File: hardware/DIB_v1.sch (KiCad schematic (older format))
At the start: 8 parts, among them IC4 M24C32-WMN6P, J1 20-pin power socket, J17 FTDI, J3 28-pin module socket

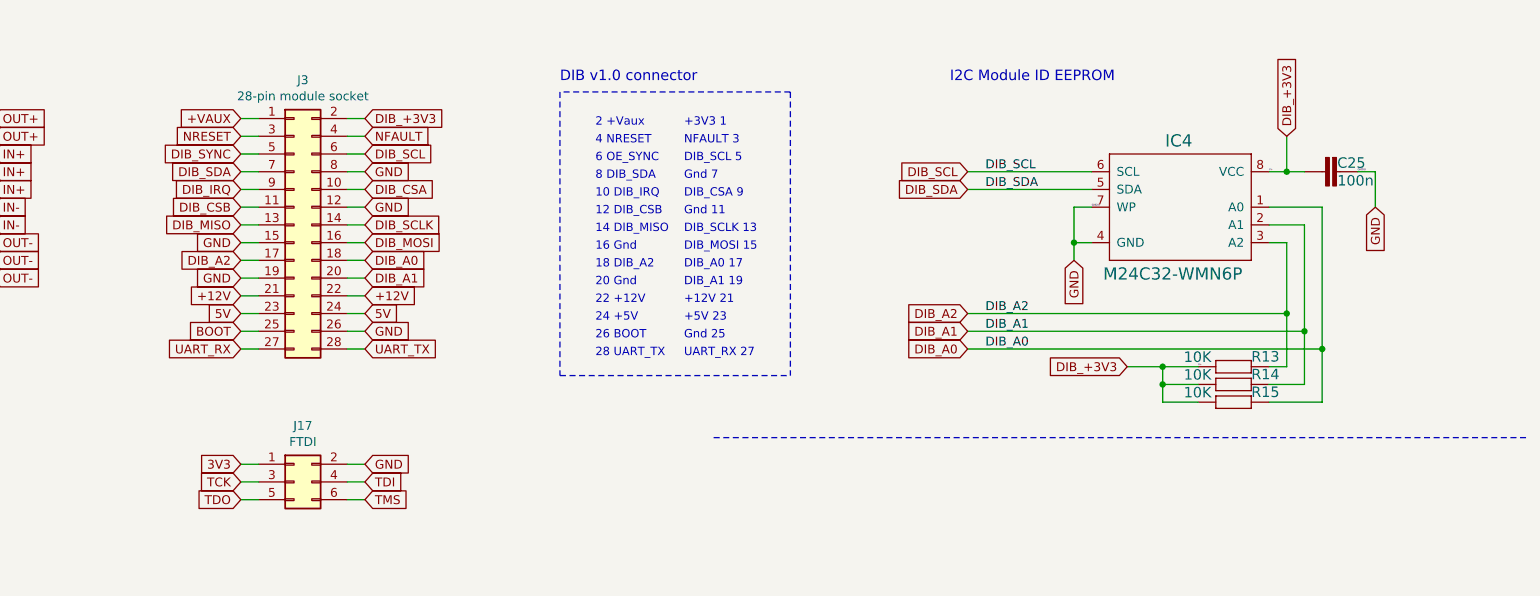
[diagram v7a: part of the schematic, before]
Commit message: Before AGND - GND
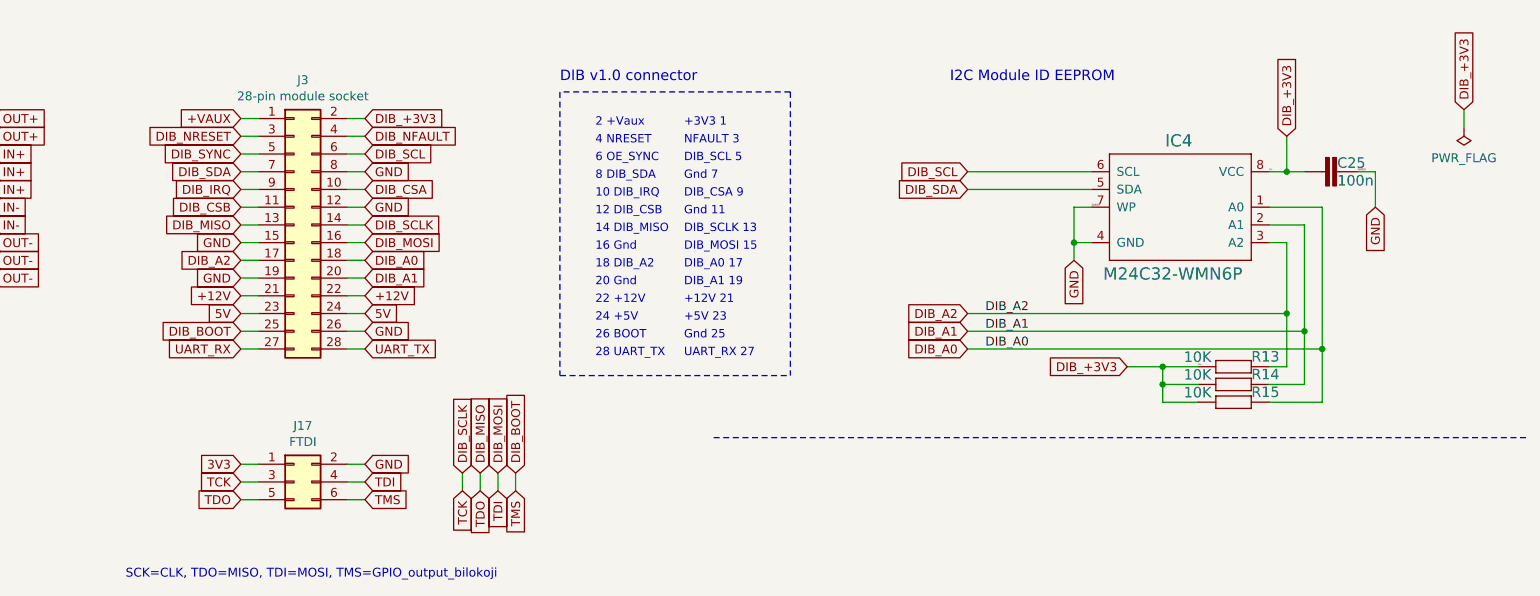
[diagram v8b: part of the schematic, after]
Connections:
- net TCK is gone; now on net DIB_SCLK: J17.3 (Pin_3)
- net TDI is gone; now on net DIB_MOSI: J17.4 (Pin_4)
- net TDO is gone; now on net DIB_MISO: J17.5 (Pin_5)
- net TMS is gone; now on net DIB_BOOT: J17.6 (Pin_6)
- net BOOT renamed DIB_BOOT
- net NFAULT renamed DIB_NFAULT
- net NRESET renamed DIB_NRESET
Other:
- note added: "SCK=CLK, TDO=MISO, TDI=MOSI, TMS=GPIO_output_bilokoji"
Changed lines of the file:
@@
 +VAUX
 Text GLabel 3600 1150 0    50   Input ~ 0
-NRESET
+DIB_NRESET
 Text GLabel 3600 1250 0    50   Input ~ 0
 DIB_SYNC
@@
 5V
 Text GLabel 3600 2250 0    50   Input ~ 0
-BOOT
+DIB_BOOT
 Text GLabel 3600 2350 0    50   Input ~ 0
 UART_RX
@@
 DIB_+3V3
 Text GLabel 4300 1150 2    50   Input ~ 0
-NFAULT
+DIB_NFAULT
 Text GLabel 4300 1250 2    50   Input ~ 0
 DIB_SCL
@@
 DIB_A2
 Connection ~ 9500 2150
-Text Label 7800 1350 0    50   ~ 0
-DIB_SCL
-Text Label 7800 1450 0    50   ~ 0
-DIB_SDA
 Wire Wire Line
 	8400 1550 8300 1550
@@
 Wire Wire Line
 	4200 3200 4300 3200
+Text Notes 2950 3650 0    50   ~ 0
+SCK=CLK, TDO=MISO, TDI=MOSI, TMS=GPIO_output_bilokoji
+Text GLabel 4850 3050 1    50   Input ~ 0
+DIB_SCLK
+Text GLabel 4850 3150 3    50   Input ~ 0
+TCK
+Text GLabel 5050 3050 1    50   Input ~ 0
+DIB_MOSI
+Text GLabel 4950 3050 1    50   Input ~ 0
+DIB_MISO
+Text GLabel 4950 3150 3    50   Input ~ 0
+TDO
+Text GLabel 5050 3150 3    50   Input ~ 0
+TDI
+Text GLabel 5150 3050 1    50   Input ~ 0
+DIB_BOOT
+Text GLabel 5150 3150 3    50   Input ~ 0
+TMS
+Wire Wire Line
+	4850 3050 4850 3150
+Wire Wire Line
+	4950 3050 4950 3150
+Wire Wire Line
+	5050 3050 5050 3150
+Wire Wire Line
+	5150 3050 5150 3150
+Text GLabel 10500 1000 1    50   Input ~ 0
+DIB_+3V3
+$Comp
+L power:PWR_FLAG #FLG0105
+U 1 1 5E70951C
+P 10500 1100
+F 0 "#FLG0105" H 10500 1175 50  0001 C CNN
+F 1 "PWR_FLAG" H 10500 1273 50  0000 C CNN
+F 2 "" H 10500 1100 50  0001 C CNN
+F 3 "~" H 10500 1100 50  0001 C CNN
+	1    10500 1100
+	-1   0    0    1
+$EndComp
+Wire Wire Line
+	10500 1000 10500 1100
 $EndSCHEMATC
